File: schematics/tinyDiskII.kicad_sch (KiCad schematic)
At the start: 51 parts, among them J1 AVR-PDI-6, J2 SD_Card, J3 USB_B_Mini, J4 APPLEII_DISK_CONNECTOR, J5 Ext, SW1 RotaryEncoder_Switch, U1 MX25R3235FM1xx0, U10 AP1117-33, U2 SN74LVC244, U3 CH340C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

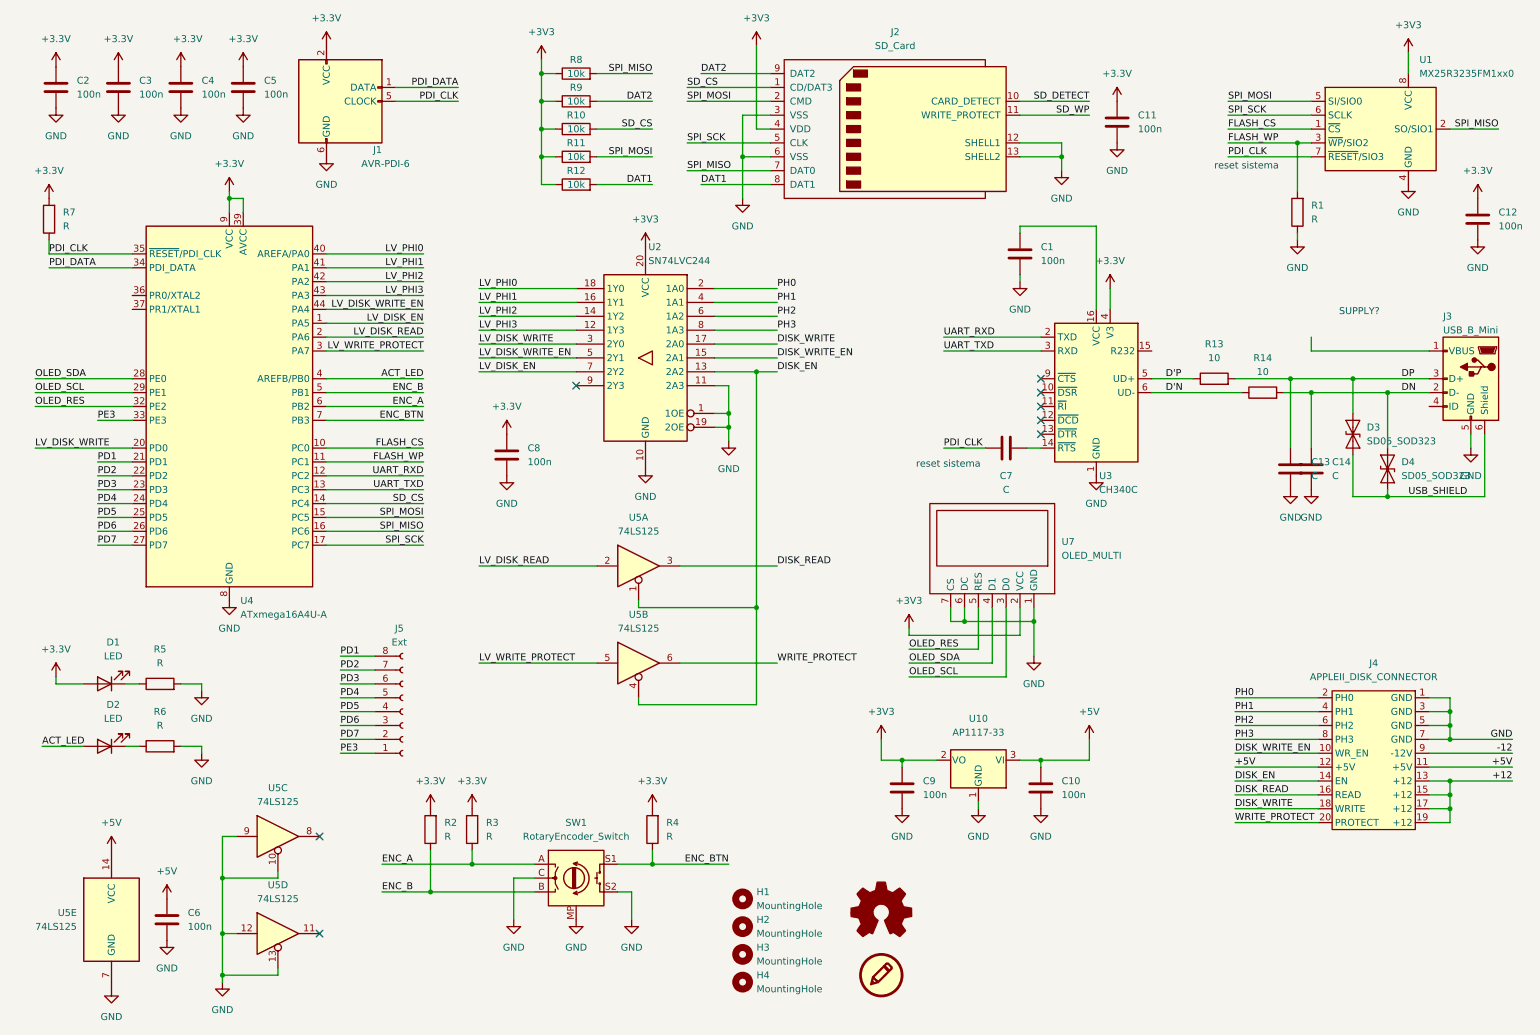
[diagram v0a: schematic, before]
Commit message: [schematics] Removed some notes from schematic
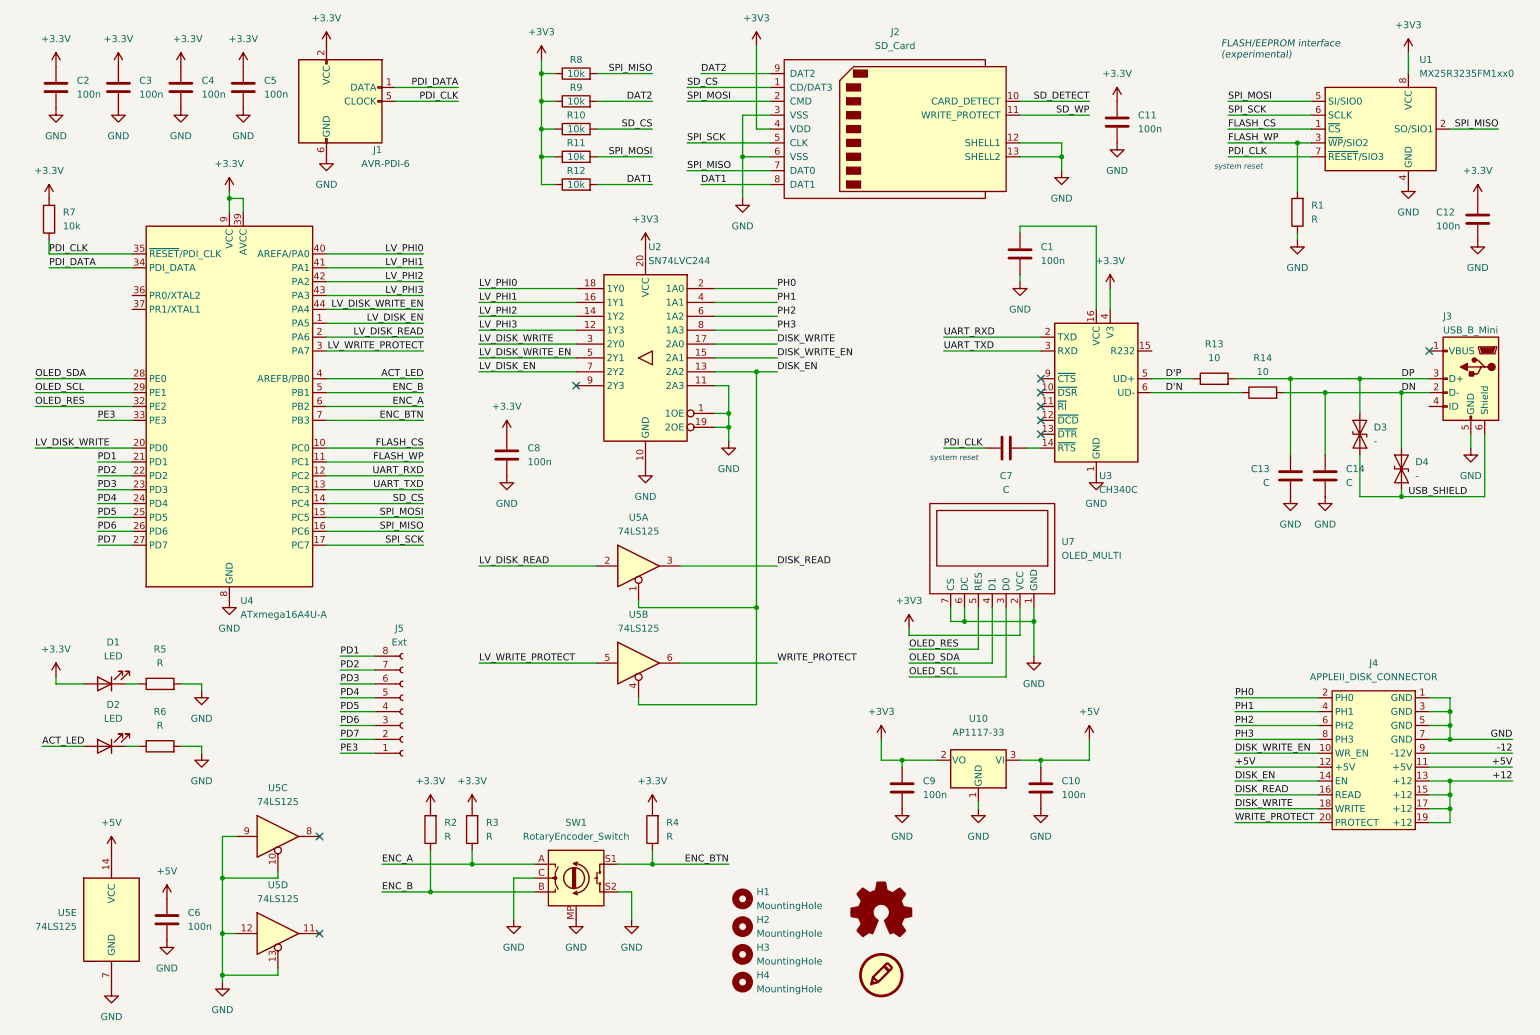
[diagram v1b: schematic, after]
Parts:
- D3, D4: value SD05_SOD323 -> -
- R7: value R -> 10k
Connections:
- no-connect marks 8 -> 9
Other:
- note added: "FLASH/EEPROM interface (experimental)"
- note added: "system reset"
- note removed: "SUPPLY?"
- note removed: "reset sistema"
- moved on the sheet: C13, C14, D3, D4

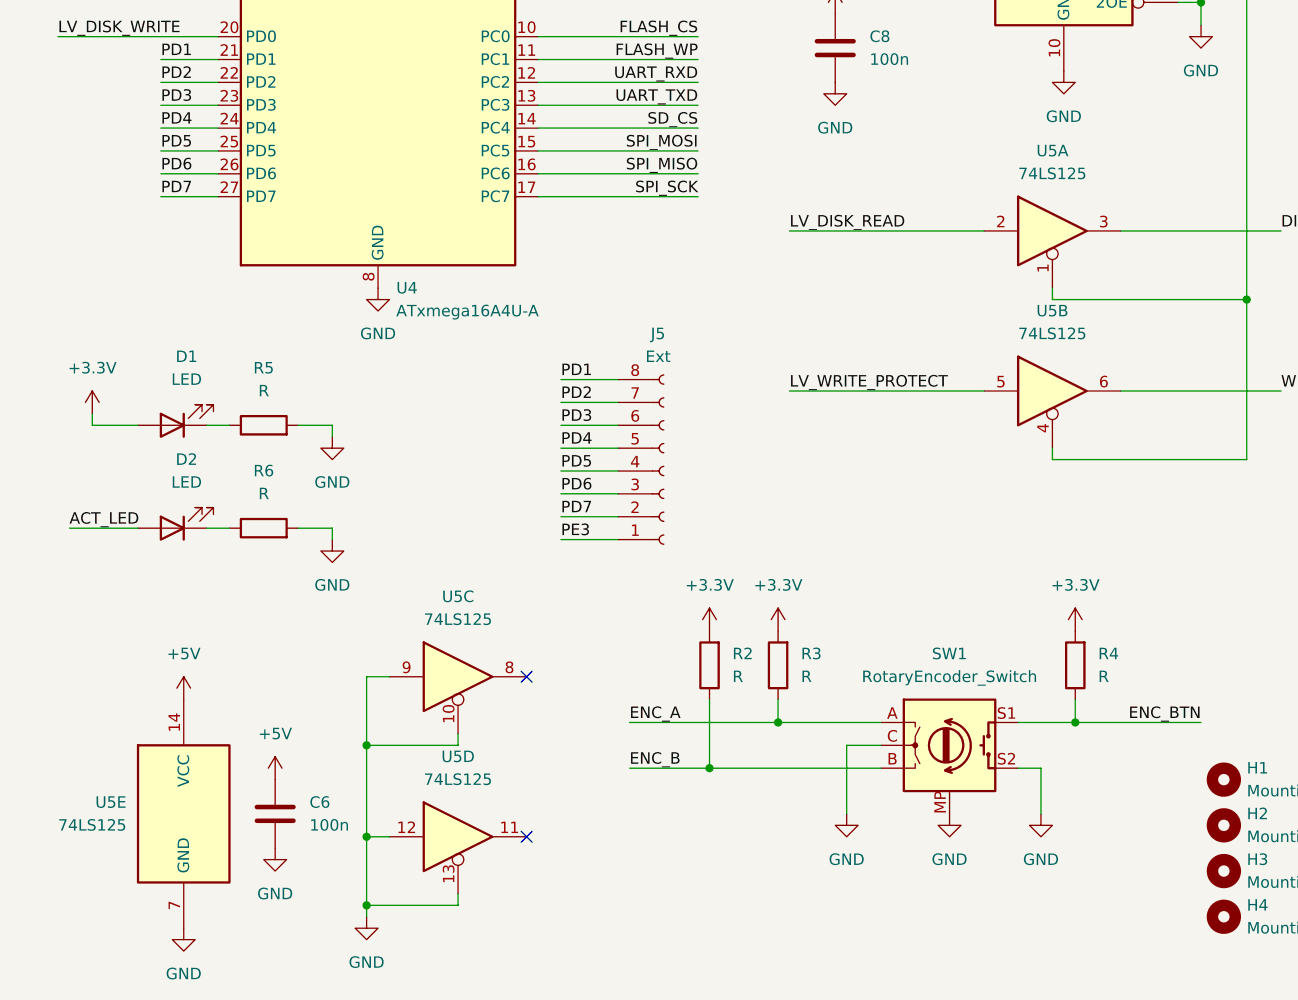
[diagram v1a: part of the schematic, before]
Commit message: [schematics] Updated missing values
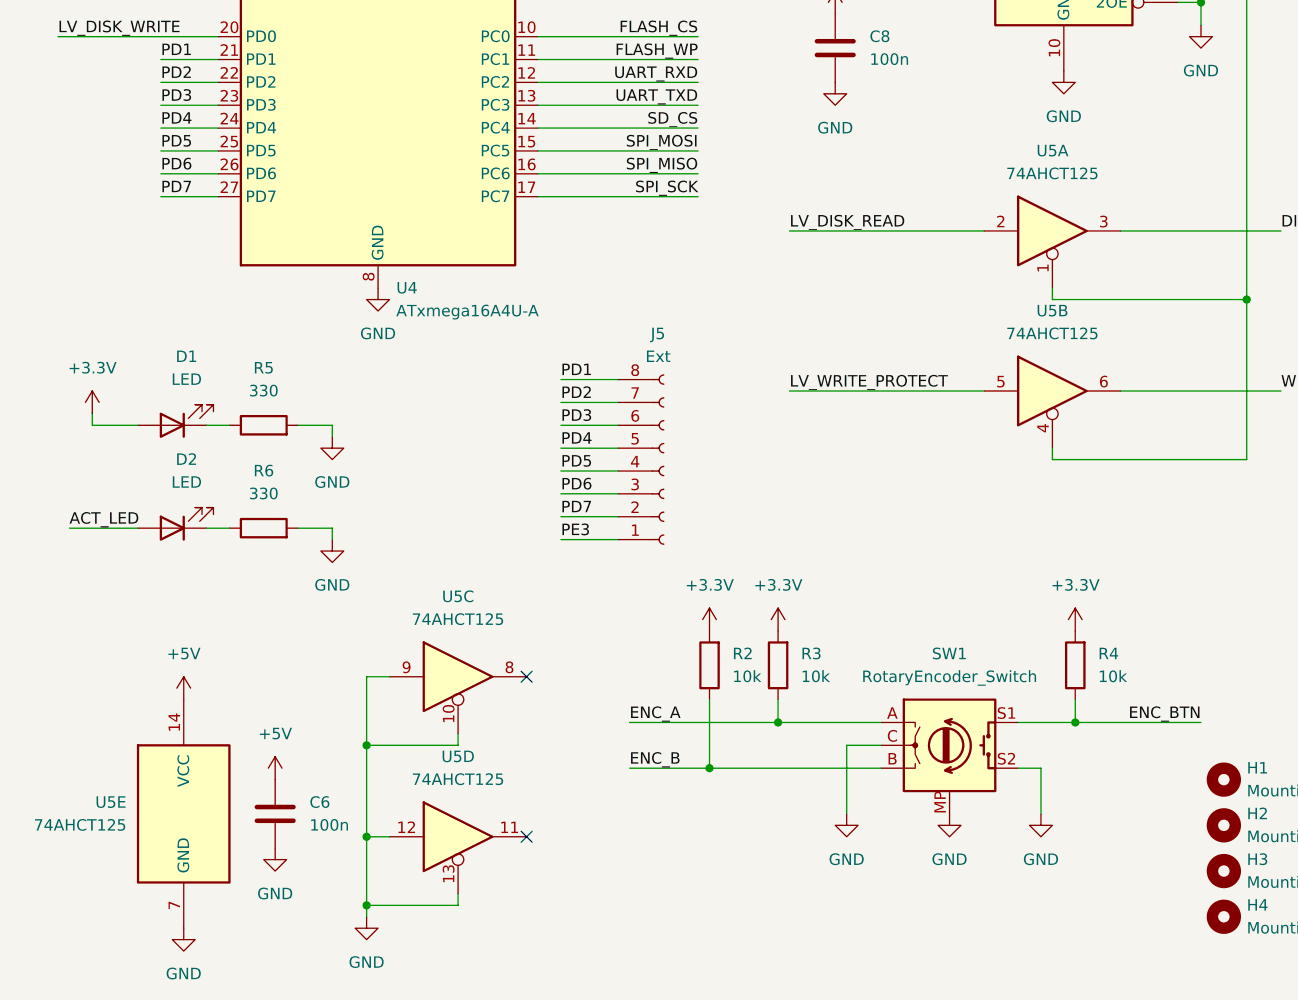
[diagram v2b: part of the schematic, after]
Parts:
- R2, R3, R4: value R -> 10k
- R5, R6: value R -> 330
- U5: value 74LS125 -> 74AHCT125
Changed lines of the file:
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@@
       (effects (font (size 1.27 1.27)) (justify right))
     )
-    (property "Value" "R" (id 1) (at 96.52 163.8299 0)
+    (property "Value" "10k" (id 1) (at 96.52 163.8299 0)
       (effects (font (size 1.27 1.27)) (justify right))
     )
@@
     (in_bom yes) (on_board yes) (fields_autoplaced)
     (property "Reference" "U5" (id 0) (at 124.46 105.41 0))
-    (property "Value" "74LS125" (id 1) (at 124.46 107.95 0))
+    (property "Value" "74AHCT125" (id 1) (at 124.46 107.95 0))
     (property "Footprint" "Package_SO:SOIC-14_3.9x8.7mm_P1.27mm" (id 2) (at 124.46 114.3 0)
       (effects (font (size 1.27 1.27)) hide)
@@
       (effects (font (size 1.27 1.27)) (justify right))
     )
-    (property "Value" "74LS125" (id 1) (at 21.59 180.3399 0)
+    (property "Value" "74AHCT125" (id 1) (at 21.59 180.3399 0)
       (effects (font (size 1.27 1.27)) (justify right))
     )
@@
     (in_bom yes) (on_board yes) (fields_autoplaced)
     (property "Reference" "R6" (id 0) (at 36.83 140.97 90))
-    (property "Value" "R" (id 1) (at 36.83 143.51 90))
+    (property "Value" "330" (id 1) (at 36.83 143.51 90))
     (property "Footprint" "Resistor_SMD:R_0805_2012Metric" (id 2) (at 36.83 149.098 90)
       (effects (font (size 1.27 1.27)) hide)
@@
     (in_bom yes) (on_board yes) (fields_autoplaced)
     (property "Reference" "U5" (id 0) (at 124.46 123.19 0))
-    (property "Value" "74LS125" (id 1) (at 124.46 125.73 0))
+    (property "Value" "74AHCT125" (id 1) (at 124.46 125.73 0))
     (property "Footprint" "Package_SO:SOIC-14_3.9x8.7mm_P1.27mm" (id 2) (at 124.46 132.08 0)
       (effects (font (size 1.27 1.27)) hide)
@@
       (effects (font (size 1.27 1.27)) (justify right))
     )
-    (property "Value" "R" (id 1) (at 88.9 163.8299 0)
+    (property "Value" "10k" (id 1) (at 88.9 163.8299 0)
       (effects (font (size 1.27 1.27)) (justify right))
     )
@@
       (effects (font (size 1.27 1.27)) (justify right))
     )
-    (property "Value" "R" (id 1) (at 129.54 163.8299 0)
+    (property "Value" "10k" (id 1) (at 129.54 163.8299 0)
       (effects (font (size 1.27 1.27)) (justify right))
     )
@@
     (in_bom yes) (on_board yes) (fields_autoplaced)
     (property "Reference" "U5" (id 0) (at 58.42 154.94 0))
-    (property "Value" "74LS125" (id 1) (at 58.42 157.48 0))
+    (property "Value" "74AHCT125" (id 1) (at 58.42 157.48 0))
     (property "Footprint" "Package_SO:SOIC-14_3.9x8.7mm_P1.27mm" (id 2) (at 58.42 163.83 0)
       (effects (font (size 1.27 1.27)) hide)
@@
     (in_bom yes) (on_board yes) (fields_autoplaced)
     (property "Reference" "R5" (id 0) (at 36.83 129.54 90))
-    (property "Value" "R" (id 1) (at 36.83 132.08 90))
+    (property "Value" "330" (id 1) (at 36.83 132.08 90))
     (property "Footprint" "Resistor_SMD:R_0805_2012Metric" (id 2) (at 36.83 137.668 90)
       (effects (font (size 1.27 1.27)) hide)
@@
     (in_bom yes) (on_board yes) (fields_autoplaced)
     (property "Reference" "U5" (id 0) (at 58.42 172.72 0))
-    (property "Value" "74LS125" (id 1) (at 58.42 175.26 0))
+    (property "Value" "74AHCT125" (id 1) (at 58.42 175.26 0))
     (property "Footprint" "Package_SO:SOIC-14_3.9x8.7mm_P1.27mm" (id 2) (at 58.42 181.61 0)
       (effects (font (size 1.27 1.27)) hide)
@@
     )
     (path "/b8c3b962-07e0-448f-b262-3034538a3e93"
-      (reference "R2") (unit 1) (value "R") (footprint "Resistor_SMD:R_0805_2012Metric")
+      (reference "R2") (unit 1) (value "10k") (footprint "Resistor_SMD:R_0805_2012Metric")
     )
     (path "/1af72c4e-3894-48fc-aaa7-a35e77814d7a"
-      (reference "R3") (unit 1) (value "R") (footprint "Resistor_SMD:R_0805_2012Metric")
+      (reference "R3") (unit 1) (value "10k") (footprint "Resistor_SMD:R_0805_2012Metric")
     )
     (path "/cd6c0189-d003-4535-9bcf-c3ca22142ab9"
-      (reference "R4") (unit 1) (value "R") (footprint "Resistor_SMD:R_0805_2012Metric")
+      (reference "R4") (unit 1) (value "10k") (footprint "Resistor_SMD:R_0805_2012Metric")
     )
     (path "/fca1b0a0-b07f-4100-8ce5-8d5e9aec4748"
-      (reference "R5") (unit 1) (value "R") (footprint "Resistor_SMD:R_0805_2012Metric")
+      (reference "R5") (unit 1) (value "330") (footprint "Resistor_SMD:R_0805_2012Metric")
     )
     (path "/5e9919bf-e3c1-4828-be15-c0fc13e5a9b5"
-      (reference "R6") (unit 1) (value "R") (footprint "Resistor_SMD:R_0805_2012Metric")
+      (reference "R6") (unit 1) (value "330") (footprint "Resistor_SMD:R_0805_2012Metric")
     )
     (path "/5955f9b4-0c8e-4d29-858a-0f7264e950d9"
@@
     )
     (path "/3179b286-c79a-430d-987c-b7813d5141f2"
-      (reference "U5") (unit 1) (value "74LS125") (footprint "Package_SO:SOIC-14_3.9x8.7mm_P1.27mm")
+      (reference "U5") (unit 1) (value "74AHCT125") (footprint "Package_SO:SOIC-14_3.9x8.7mm_P1.27mm")
     )
     (path "/ab6e4982-4967-49f2-bce0-bafa1288ccc7"
-      (reference "U5") (unit 2) (value "74LS125") (footprint "Package_SO:SOIC-14_3.9x8.7mm_P1.27mm")
+      (reference "U5") (unit 2) (value "74AHCT125") (footprint "Package_SO:SOIC-14_3.9x8.7mm_P1.27mm")
     )
     (path "/db2092c2-4740-4538-ad8f-c08811bf4330"
-      (reference "U5") (unit 3) (value "74LS125") (footprint "Package_SO:SOIC-14_3.9x8.7mm_P1.27mm")
+      (reference "U5") (unit 3) (value "74AHCT125") (footprint "Package_SO:SOIC-14_3.9x8.7mm_P1.27mm")
     )
     (path "/fd03c159-b804-4d74-aed8-f9a54c79590e"
-      (reference "U5") (unit 4) (value "74LS125") (footprint "Package_SO:SOIC-14_3.9x8.7mm_P1.27mm")
+      (reference "U5") (unit 4) (value "74AHCT125") (footprint "Package_SO:SOIC-14_3.9x8.7mm_P1.27mm")
     )
     (path "/38bcc7dc-93f9-46d7-b291-255f5c5a956f"
-      (reference "U5") (unit 5) (value "74LS125") (footprint "Package_SO:SOIC-14_3.9x8.7mm_P1.27mm")
+      (reference "U5") (unit 5) (value "74AHCT125") (footprint "Package_SO:SOIC-14_3.9x8.7mm_P1.27mm")
     )
     (path "/06e13ea7-7d8c-41af-8cf5-db600411cb89"
